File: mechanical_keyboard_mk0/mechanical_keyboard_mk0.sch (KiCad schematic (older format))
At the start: 0 parts

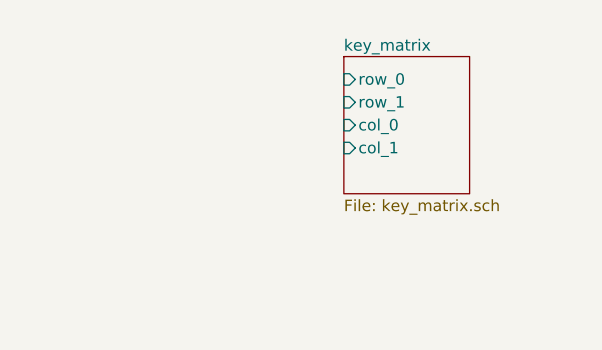
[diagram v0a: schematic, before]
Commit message: Updated to 2 rows.
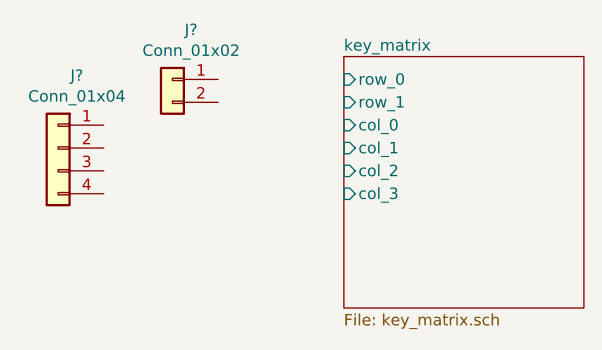
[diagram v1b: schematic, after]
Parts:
- added J?: Conn_01x04, symbol Connector_Generic:Conn_01x04
- added J?: Conn_01x02, symbol Connector_Generic:Conn_01x02
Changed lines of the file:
@@
 $EndDescr
 $Sheet
-S 5950 900  550  600
+S 5950 900  1050 1100
 U 5CEB265E
 F0 "key_matrix" 50
@@
 F4 "col_0" I L 5950 1200 50
 F5 "col_1" I L 5950 1300 50
+F6 "col_2" I L 5950 1400 50
+F7 "col_3" I L 5950 1500 50
 $EndSheet
+$Comp
+L Connector_Generic:Conn_01x04 J?
+U 1 1 5CF11413
+P 4700 1300
+F 0 "J?" H 4618 1617 50  0000 C CNN
+F 1 "Conn_01x04" H 4618 1526 50  0000 C CNN
+F 2 "" H 4700 1300 50  0001 C CNN
+F 3 "~" H 4700 1300 50  0001 C CNN
+	1    4700 1300
+	-1   0    0    -1
+$EndComp
+$Comp
+L Connector_Generic:Conn_01x02 J?
+U 1 1 5CF123CE
+P 5200 1000
+F 0 "J?" H 5118 1217 50  0000 C CNN
+F 1 "Conn_01x02" H 5118 1126 50  0000 C CNN
+F 2 "" H 5200 1000 50  0001 C CNN
+F 3 "~" H 5200 1000 50  0001 C CNN
+	1    5200 1000
+	-1   0    0    -1
+$EndComp
 $EndSCHEMATC

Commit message: Updated layout, created first output job.
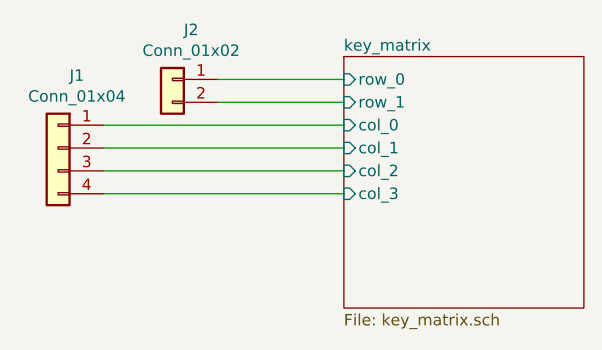
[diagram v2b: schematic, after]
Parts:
- J1: renamed from J?; footprint (none) -> Connector_PinHeader_2.54mm:PinHeader_1x04_P2.54mm_Vertical
- J2: renamed from J?; footprint (none) -> Connector_PinHeader_2.54mm:PinHeader_1x02_P2.54mm_Vertical
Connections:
- net key_matrix/col_0: now also J1.1 (Pin_1)
- net key_matrix/col_1: now also J1.2 (Pin_2)
- net key_matrix/col_2: now also J1.3 (Pin_3)
- net key_matrix/col_3: now also J1.4 (Pin_4)
- net key_matrix/row_0: now also J2.1 (Pin_1)
- net key_matrix/row_1: now also J2.2 (Pin_2)
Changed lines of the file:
@@
 $EndSheet
 $Comp
-L Connector_Generic:Conn_01x04 J?
+L Connector_Generic:Conn_01x04 J1
 U 1 1 5CF11413
 P 4700 1300
-F 0 "J?" H 4618 1617 50  0000 C CNN
+F 0 "J1" H 4618 1617 50  0000 C CNN
 F 1 "Conn_01x04" H 4618 1526 50  0000 C CNN
-F 2 "" H 4700 1300 50  0001 C CNN
+F 2 "Connector_PinHeader_2.54mm:PinHeader_1x04_P2.54mm_Vertical" H 4700 1300 50  0001 C CNN
 F 3 "~" H 4700 1300 50  0001 C CNN
 	1    4700 1300
@@
 $EndComp
 $Comp
-L Connector_Generic:Conn_01x02 J?
+L Connector_Generic:Conn_01x02 J2
 U 1 1 5CF123CE
 P 5200 1000
-F 0 "J?" H 5118 1217 50  0000 C CNN
+F 0 "J2" H 5118 1217 50  0000 C CNN
 F 1 "Conn_01x02" H 5118 1126 50  0000 C CNN
-F 2 "" H 5200 1000 50  0001 C CNN
+F 2 "Connector_PinHeader_2.54mm:PinHeader_1x02_P2.54mm_Vertical" H 5200 1000 50  0001 C CNN
 F 3 "~" H 5200 1000 50  0001 C CNN
 	1    5200 1000
 	-1   0    0    -1
 $EndComp
+Wire Wire Line
+	5400 1000 5950 1000
+Wire Wire Line
+	5400 1100 5950 1100
+Wire Wire Line
+	4900 1200 5950 1200
+Wire Wire Line
+	5950 1300 4900 1300
+Wire Wire Line
+	4900 1400 5950 1400
+Wire Wire Line
+	5950 1500 4900 1500
 $EndSCHEMATC
